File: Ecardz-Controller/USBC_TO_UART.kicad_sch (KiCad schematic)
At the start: 11 parts, among them J3 Conn_01x04, U4 CP2110-F02-GM1

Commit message: initial work on controller layout
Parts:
- renumbered C7 to C37, C10 to C38, C8 to C39, C11 to C40, C9 to C41, J3 to J8, R17 to R38, R18 to R39, TP5 to TP8, TP6 to TP9
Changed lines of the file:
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@@
 		(on_board yes)
 		(dnp no)
-		(property "Reference" "C10"
+		(property "Reference" "C38"
 			(at 90.17 32.766 0)
 			(effects
@@
 			(project "Ecardz-Controller"
 				(path "/74270717-a116-451e-ac88-5a07ab66056e/795903a0-6fb6-4696-956b-ef2670233793"
-					(reference "C10")
+					(reference "C38")
 					(unit 1)
 				)
@@
 		(dnp no)
 		(fields_autoplaced yes)
-		(property "Reference" "#PWR012"
+		(property "Reference" "#PWR048"
 			(at 116.84 111.76 0)
 			(effects
@@
 			(project "Ecardz-Controller"
 				(path "/74270717-a116-451e-ac88-5a07ab66056e/795903a0-6fb6-4696-956b-ef2670233793"
-					(reference "#PWR012")
+					(reference "#PWR048")
 					(unit 1)
 				)
@@
 		(dnp no)
 		(fields_autoplaced yes)
-		(property "Reference" "TP6"
+		(property "Reference" "TP9"
 			(at 149.86 61.4679 0)
 			(effects
@@
 			(project "Ecardz-Controller"
 				(path "/74270717-a116-451e-ac88-5a07ab66056e/795903a0-6fb6-4696-956b-ef2670233793"
-					(reference "TP6")
+					(reference "TP9")
 					(unit 1)
 				)
@@
 		(on_board yes)
 		(dnp no)
-		(property "Reference" "C9"
+		(property "Reference" "C41"
 			(at 184.404 35.052 0)
 			(effects
@@
 			(project "Ecardz-Controller"
 				(path "/74270717-a116-451e-ac88-5a07ab66056e/795903a0-6fb6-4696-956b-ef2670233793"
-					(reference "C9")
+					(reference "C41")
 					(unit 1)
 				)
@@
 		(dnp no)
 		(fields_autoplaced yes)
-		(property "Reference" "#PWR015"
+		(property "Reference" "#PWR047"
 			(at 88.9 49.53 0)
 			(effects
@@
 			(project "Ecardz-Controller"
 				(path "/74270717-a116-451e-ac88-5a07ab66056e/795903a0-6fb6-4696-956b-ef2670233793"
-					(reference "#PWR015")
+					(reference "#PWR047")
 					(unit 1)
 				)
@@
 		(dnp no)
 		(fields_autoplaced yes)
-		(property "Reference" "C8"
+		(property "Reference" "C39"
 			(at 144.78 80.0099 0)
 			(effects
@@
 			(project "Ecardz-Controller"
 				(path "/74270717-a116-451e-ac88-5a07ab66056e/795903a0-6fb6-4696-956b-ef2670233793"
-					(reference "C8")
+					(reference "C39")
 					(unit 1)
 				)
@@
 		(dnp no)
 		(fields_autoplaced yes)
-		(property "Reference" "R17"
+		(property "Reference" "R38"
 			(at 140.97 34.29 90)
 			(effects
@@
 			(project "Ecardz-Controller"
 				(path "/74270717-a116-451e-ac88-5a07ab66056e/795903a0-6fb6-4696-956b-ef2670233793"
-					(reference "R17")
+					(reference "R38")
 					(unit 1)
 				)
@@
 		(dnp no)
 		(fields_autoplaced yes)
-		(property "Reference" "TP5"
+		(property "Reference" "TP8"
 			(at 137.16 58.9279 0)
 			(effects
@@
 			(project "Ecardz-Controller"
 				(path "/74270717-a116-451e-ac88-5a07ab66056e/795903a0-6fb6-4696-956b-ef2670233793"
-					(reference "TP5")
+					(reference "TP8")
 					(unit 1)
 				)
@@
 		(dnp no)
 		(fields_autoplaced yes)
-		(property "Reference" "#PWR014"
+		(property "Reference" "#PWR050"
 			(at 173.99 55.88 0)
 			(effects
@@
 			(project "Ecardz-Controller"
 				(path "/74270717-a116-451e-ac88-5a07ab66056e/795903a0-6fb6-4696-956b-ef2670233793"
-					(reference "#PWR014")
+					(reference "#PWR050")
 					(unit 1)
 				)
@@
 		(dnp no)
 		(fields_autoplaced yes)
-		(property "Reference" "C11"
+		(property "Reference" "C40"
 			(at 173.99 36.8299 0)
 			(effects
@@
 			(project "Ecardz-Controller"
 				(path "/74270717-a116-451e-ac88-5a07ab66056e/795903a0-6fb6-4696-956b-ef2670233793"
-					(reference "C11")
+					(reference "C40")
 					(unit 1)
 				)
@@
 		(dnp no)
 		(fields_autoplaced yes)
-		(property "Reference" "#PWR011"
+		(property "Reference" "#PWR046"
 			(at 45.72 45.72 0)
 			(effects
@@
 			(project "Ecardz-Controller"
 				(path "/74270717-a116-451e-ac88-5a07ab66056e/795903a0-6fb6-4696-956b-ef2670233793"
-					(reference "#PWR011")
+					(reference "#PWR046")
 					(unit 1)
 				)
@@
 		(dnp no)
 		(fields_autoplaced yes)
-		(property "Reference" "#PWR013"
+		(property "Reference" "#PWR049"
 			(at 140.97 97.79 0)
 			(effects
@@
 			(project "Ecardz-Controller"
 				(path "/74270717-a116-451e-ac88-5a07ab66056e/795903a0-6fb6-4696-956b-ef2670233793"
-					(reference "#PWR013")
+					(reference "#PWR049")
 					(unit 1)
 				)
@@
 		(on_board yes)
 		(dnp no)
-		(property "Reference" "R18"
+		(property "Reference" "R39"
 			(at 140.97 45.466 90)
 			(effects
@@
 			(project "Ecardz-Controller"
 				(path "/74270717-a116-451e-ac88-5a07ab66056e/795903a0-6fb6-4696-956b-ef2670233793"
-					(reference "R18")
+					(reference "R39")
 					(unit 1)
 				)
@@
 		(on_board yes)
 		(dnp no)
-		(property "Reference" "C7"
+		(property "Reference" "C37"
 			(at 78.994 32.512 0)
 			(effects
@@
 			(project "Ecardz-Controller"
 				(path "/74270717-a116-451e-ac88-5a07ab66056e/795903a0-6fb6-4696-956b-ef2670233793"
-					(reference "C7")
+					(reference "C37")
 					(unit 1)
 				)
@@
 		(dnp no)
 		(fields_autoplaced yes)
-		(property "Reference" "J3"
+		(property "Reference" "J8"
 			(at 38.1 22.86 0)
 			(effects
@@
 			(project "Ecardz-Controller"
 				(path "/74270717-a116-451e-ac88-5a07ab66056e/795903a0-6fb6-4696-956b-ef2670233793"
-					(reference "J3")
-					(unit 1)
-				)
+					(reference "J8")
+					(unit 1)
+				)

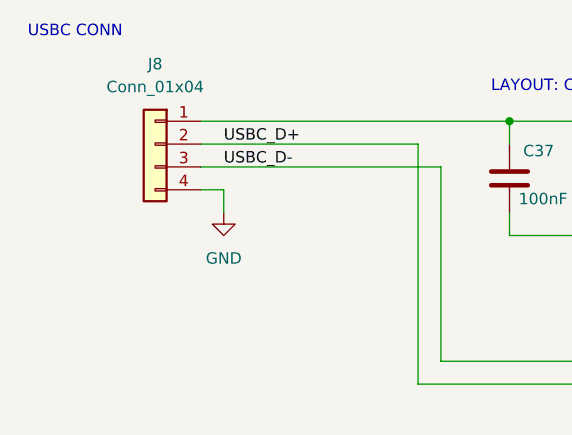
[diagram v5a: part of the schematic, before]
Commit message: did bulk of controller layout apart from the antenna, added some NCs and other minor clean ups on schematic
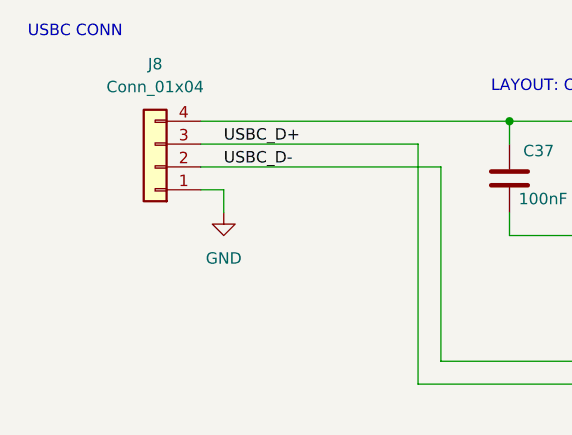
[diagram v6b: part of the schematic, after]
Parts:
- J8: footprint (none) -> Connector_PinHeader_2.54mm:PinHeader_1x04_P2.54mm_Vertical
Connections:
- net 5V_USBC: now also J8.4 (Pin_4); no longer J8.1 (Pin_1)
- net GND: now also J8.1 (Pin_1); no longer J8.4 (Pin_4)
- net USBC_D+: now also J8.3 (Pin_3); no longer J8.2 (Pin_2)
- net USBC_D-: now also J8.2 (Pin_2); no longer J8.3 (Pin_3)
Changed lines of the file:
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@@
+	)
+	(symbol
+		(lib_id "Connector_Generic:Conn_01x04")
+		(at 38.1 34.29 180)
+		(unit 1)
+		(exclude_from_sim no)
+		(in_bom yes)
+		(on_board yes)
+		(dnp no)
+		(fields_autoplaced yes)
+		(property "Reference" "J8"
+			(at 38.1 22.86 0)
+			(effects
+				(font
+					(size 1.27 1.27)
+				)
+			)
+		)
+		(property "Value" "Conn_01x04"
+			(at 38.1 25.4 0)
+			(effects
+				(font
+					(size 1.27 1.27)
+				)
+			)
+		)
+		(property "Footprint" "Connector_PinHeader_2.54mm:PinHeader_1x04_P2.54mm_Vertical"
+			(at 38.1 34.29 0)
+			(effects
+				(font
+					(size 1.27 1.27)
+				)
+				(hide yes)
+			)
+		)
+		(property "Datasheet" "~"
+			(at 38.1 34.29 0)
+			(effects
+				(font
+					(size 1.27 1.27)
+				)
+				(hide yes)
+			)
+		)
+		(property "Description" "Generic connector, single row, 01x04, script generated (kicad-library-utils/schlib/autogen/connector/)"
+			(at 38.1 34.29 0)
+			(effects
+				(font
+					(size 1.27 1.27)
+				)
+				(hide yes)
+			)
+		)
+		(pin "3"
+		)
+		(pin "1"
+		)
+		(pin "4"
+		)
+		(pin "2"
+		)
+		(instances
+			(project ""
+				(path "/74270717-a116-451e-ac88-5a07ab66056e/795903a0-6fb6-4696-956b-ef2670233793"
+					(reference "J8")
+					(unit 1)
+				)
+			)
+		)
 	)
 	(symbol
@@
 					(unit 1)
 				)
-			)
-		)
-	)
-	(symbol
-		(lib_id "Connector_Generic:Conn_01x04")
-		(at 38.1 31.75 0)
-		(mirror y)
-		(unit 1)
-		(exclude_from_sim no)
-		(in_bom yes)
-		(on_board yes)
-		(dnp no)
-		(fields_autoplaced yes)
-		(property "Reference" "J8"
-			(at 38.1 22.86 0)
-			(effects
-				(font
-					(size 1.27 1.27)
-				)
-			)
-		)
-		(property "Value" "Conn_01x04"
-			(at 38.1 25.4 0)
-			(effects
-				(font
-					(size 1.27 1.27)
-				)
-			)
-		)
-		(property "Footprint" ""
-			(at 38.1 31.75 0)
-			(effects
-				(font
-					(size 1.27 1.27)
-				)
-				(hide yes)
-			)
-		)
-		(property "Datasheet" "~"
-			(at 38.1 31.75 0)
-			(effects
-				(font
-					(size 1.27 1.27)
-				)
-				(hide yes)
-			)
-		)
-		(property "Description" "Generic connector, single row, 01x04, script generated (kicad-library-utils/schlib/autogen/connector/)"
-			(at 38.1 31.75 0)
-			(effects
-				(font
-					(size 1.27 1.27)
-				)
-				(hide yes)
-			)
-		)
-		(pin "3"
-		)
-		(pin "2"
-		)
-		(pin "1"
-		)
-		(pin "4"
-		)
-		(instances
-			(project "Ecardz-Controller"
-				(path "/74270717-a116-451e-ac88-5a07ab66056e/795903a0-6fb6-4696-956b-ef2670233793"
-					(reference "J8")
-					(unit 1)
-				)

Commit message: controller updates
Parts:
- added TP15, TP16: TestPoint, TestPoint:TestPoint_Pad_D3.0mm, symbol Connector:TestPoint
- C37, C41: value 100nF -> 100n
- J8: Part Number (none) -> 61300411121
- R39: renamed from R38; Part Number (none) -> RMCF0603ZT0R00
- R40: renamed from R39; Part Number (none) -> RMCF0603ZT0R00
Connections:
- net 5V_USBC: now also TP15.1
- net GND: now also TP16.1

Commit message: changed headers to 90 degree angled headers
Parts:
- J8: footprint Connector_PinHeader_2.54mm:PinHeader_1x04_P2.54mm_Vertical -> Connector_PinHeader_2.54mm:PinHeader_1x04_P2.54mm_Horizontal
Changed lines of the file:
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@@
 			)
 		)
-		(property "Footprint" "Connector_PinHeader_2.54mm:PinHeader_1x04_P2.54mm_Vertical"
+		(property "Footprint" "Connector_PinHeader_2.54mm:PinHeader_1x04_P2.54mm_Horizontal"
 			(at 38.1 34.29 0)
 			(effects
